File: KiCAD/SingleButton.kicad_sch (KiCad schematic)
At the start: 2 parts

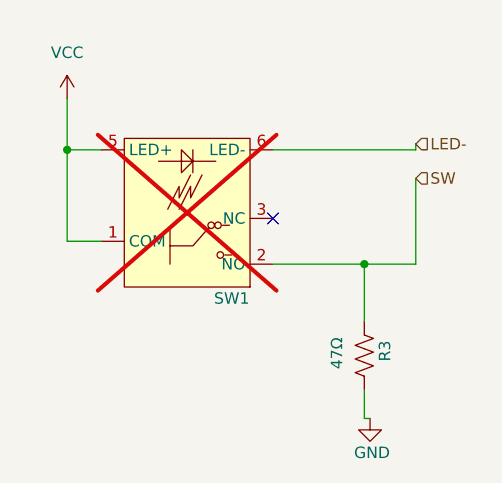
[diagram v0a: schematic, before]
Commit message: 3 rows of 16 buttons; SMT
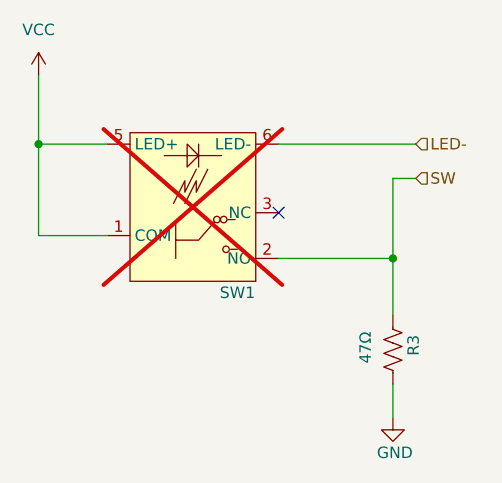
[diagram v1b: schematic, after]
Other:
- moved on the sheet: R3, SW1
